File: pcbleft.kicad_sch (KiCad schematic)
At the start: 38 parts, among them SW1 GENERIC_ELECTROMECHANICAL_PUS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, SW10 GENERIC_ELECTROMECHANICAL_PUS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, SW11 GENERIC_ELECTROMECHANICAL_PUS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, SW12 GENERIC_ELECTROMECHANICAL_PUS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, SW13 GENERIC_ELECTROMECHANICAL_PUS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, SW14 GENERIC_ELECTROMECHANICAL_PUS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, SW15 GENERIC_ELECTROMECHANICAL_PUS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, SW16 GENERIC_ELECTROMECHANICAL_PUS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, SW17 GENERIC_ELECTROMECHANICAL_PUS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, SW18 GENERIC_ELECTROMECHANICAL_PUS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, SW2 GENERIC_ELECTROMECHANICAL_PUS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, SW3 GENERIC_ELECTROMECHANICAL_PUS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, SW4 GENERIC_ELECTROMECHANICAL_PUS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, SW5 GENERIC_ELECTROMECHANICAL_PUS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, SW6 GENERIC_ELECTROMECHANICAL_PUS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, SW7 GENERIC_ELECTROMECHANICAL_PUS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, SW8 GENERIC_ELECTROMECHANICAL_PUS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, SW9 GENERIC_ELECTROMECHANICAL_PUS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, U1 XIAO-RP2040-DIP

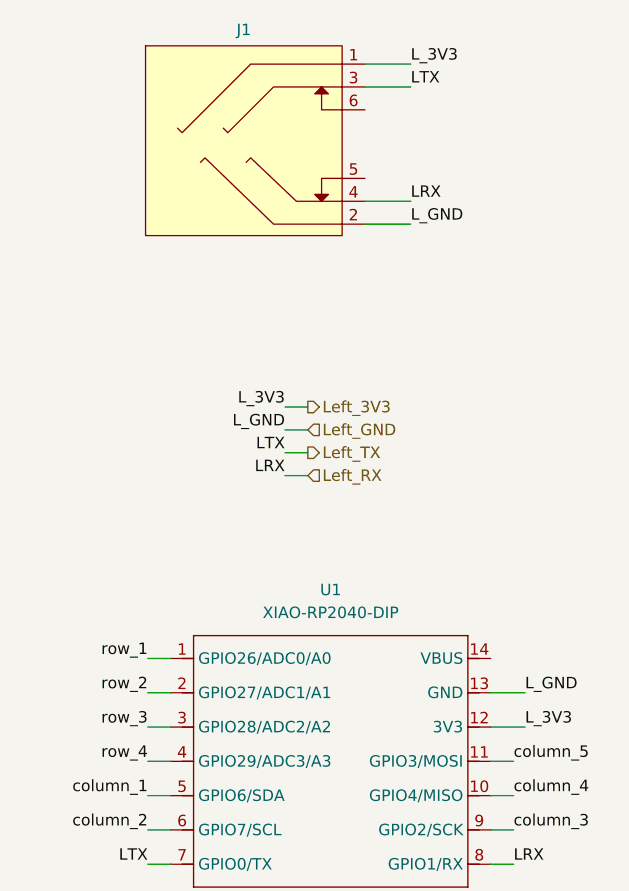
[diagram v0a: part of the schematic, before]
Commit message: Rev 1.1, fix diode footprints, add plate and base generation jobs, add mouse bites and some extra solder jumpers
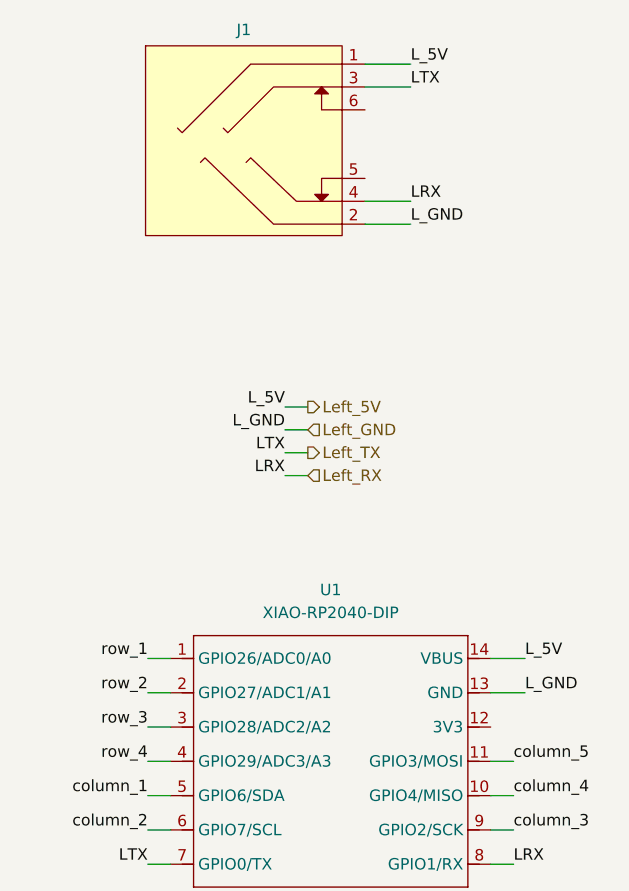
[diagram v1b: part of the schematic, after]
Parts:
- SW1, SW10, SW11, SW12, SW13, SW14, SW15, SW16, SW17, SW18, SW2, SW3, SW4, SW5, SW6, SW7, SW8, SW9: footprint benri-projects:GatereonHotswap -> benri-projects:GATEREON_KS-2P02B01-01-a_R
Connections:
- net Left_5V: now reaches U1.14 (VBUS)
- net Left_5V: now also J1.1
- net Left_3V3: no longer names the net of U1.12 (3V3)
- net Left_3V3: no longer J1.1
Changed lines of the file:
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@@
 	(wire
 		(pts
+			(xy 231.14 120.65) (xy 234.95 120.65)
+		)
+		(stroke
+			(width 0)
+			(type default)
+		)
+	)
+	(wire
+		(pts
 			(xy 135.89 71.12) (xy 135.89 73.66)
 		)
@@
 	(wire
 		(pts
-			(xy 231.14 128.27) (xy 234.95 128.27)
-		)
-		(stroke
-			(width 0)
-			(type default)
-		)
-	)
-	(wire
-		(pts
 			(xy 92.71 87.63) (xy 93.98 87.63)
 		)
@@
 		)
 	)
-	(label "L_3V3"
+	(label "L_5V"
 		(at 208.28 92.71 180)
 		(effects
@@
 		)
 	)
-	(label "L_3V3"
-		(at 234.95 128.27 0)
+	(label "L_5V"
+		(at 234.95 120.65 0)
 		(effects
 			(font
@@
 		)
 	)
-	(label "L_3V3"
+	(label "L_5V"
 		(at 222.25 54.61 0)
 		(effects
@@
 		)
 	)
-	(hierarchical_label "Left_3V3"
+	(hierarchical_label "Left_5V"
 		(shape output)
 		(at 210.82 92.71 0)
@@
 			)
 		)
-		(property "Footprint" "benri-projects:GatereonHotswap"
+		(property "Footprint" "benri-projects:GATEREON_KS-2P02B01-01-a_R"
 			(at 124.46 99.06 0)
 			(effects
@@
 			)
 		)
-		(property "Footprint" "benri-projects:GatereonHotswap"
+		(property "Footprint" "benri-projects:GATEREON_KS-2P02B01-01-a_R"
 			(at 124.46 82.55 0)
 			(effects
@@
 			)
 		)
-		(property "Footprint" "benri-projects:GatereonHotswap"
+		(property "Footprint" "benri-projects:GATEREON_KS-2P02B01-01-a_R"
 			(at 68.58 82.55 0)
 			(effects
@@
 			)
 		)
-		(property "Footprint" "benri-projects:GatereonHotswap"
+		(property "Footprint" "benri-projects:GATEREON_KS-2P02B01-01-a_R"
 			(at 87.63 82.55 0)
 			(effects
@@
 			)
 		)
-		(property "Footprint" "benri-projects:GatereonHotswap"
+		(property "Footprint" "benri-projects:GATEREON_KS-2P02B01-01-a_R"
 			(at 124.46 115.57 0)
 			(effects
@@
 			)
 		)
-		(property "Footprint" "benri-projects:GatereonHotswap"
+		(property "Footprint" "benri-projects:GATEREON_KS-2P02B01-01-a_R"
 			(at 105.41 66.04 0)
 			(effects
@@
 			)
 		)
-		(property "Footprint" "benri-projects:GatereonHotswap"
+		(property "Footprint" "benri-projects:GATEREON_KS-2P02B01-01-a_R"
 			(at 87.63 99.06 0)
 			(effects
@@
 			)
 		)
-		(property "Footprint" "benri-projects:GatereonHotswap"
+		(property "Footprint" "benri-projects:GATEREON_KS-2P02B01-01-a_R"
 			(at 105.41 99.06 0)
 			(effects
@@
 			)
 		)
-		(property "Footprint" "benri-projects:GatereonHotswap"
+		(property "Footprint" "benri-projects:GATEREON_KS-2P02B01-01-a_R"
 			(at 143.51 66.04 0)
 			(effects
@@
 			)
 		)
-		(property "Footprint" "benri-projects:GatereonHotswap"
+		(property "Footprint" "benri-projects:GATEREON_KS-2P02B01-01-a_R"
 			(at 68.58 66.04 0)
 			(effects
@@
 			)
 		)
-		(property "Footprint" "benri-projects:GatereonHotswap"
+		(property "Footprint" "benri-projects:GATEREON_KS-2P02B01-01-a_R"
 			(at 50.8 66.04 0)
 			(effects
@@
 			)
 		)
-		(property "Footprint" "benri-projects:GatereonHotswap"
+		(property "Footprint" "benri-projects:GATEREON_KS-2P02B01-01-a_R"
 			(at 124.46 66.04 0)
 			(effects
@@
 			)
 		)
-		(property "Footprint" "benri-projects:GatereonHotswap"
+		(property "Footprint" "benri-projects:GATEREON_KS-2P02B01-01-a_R"
 			(at 87.63 66.04 0)
 			(effects
@@
 			)
 		)
-		(property "Footprint" "benri-projects:GatereonHotswap"
+		(property "Footprint" "benri-projects:GATEREON_KS-2P02B01-01-a_R"
 			(at 143.51 99.06 0)
 			(effects
@@
 			)
 		)
-		(property "Footprint" "benri-projects:GatereonHotswap"
+		(property "Footprint" "benri-projects:GATEREON_KS-2P02B01-01-a_R"
 			(at 50.8 82.55 0)
 			(effects
@@
 			)
 		)
-		(property "Footprint" "benri-projects:GatereonHotswap"
+		(property "Footprint" "benri-projects:GATEREON_KS-2P02B01-01-a_R"
 			(at 105.41 82.55 0)
 			(effects
@@
 			)
 		)
-		(property "Footprint" "benri-projects:GatereonHotswap"
+		(property "Footprint" "benri-projects:GATEREON_KS-2P02B01-01-a_R"
 			(at 143.51 82.55 0)
 			(effects
@@
 			)
 		)
-		(property "Footprint" "benri-projects:GatereonHotswap"
+		(property "Footprint" "benri-projects:GATEREON_KS-2P02B01-01-a_R"
 			(at 143.51 115.57 0)
 			(effects

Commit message: Touchups and name: Logos
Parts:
- U1: footprint Seeed Studio XIAO Series Library:XIAO-RP2040-DIP -> benri-projects:SEEED_XIAO-RP2040_T-DIP
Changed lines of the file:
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@@
 			)
 		)
-		(property "Footprint" "Seeed Studio XIAO Series Library:XIAO-RP2040-DIP"
+		(property "Footprint" "benri-projects:SEEED_XIAO-RP2040_T-DIP"
 			(at 213.868 147.828 0)
 			(effects

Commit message: Latest release
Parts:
- removed J1: ~, benri-projects:TENSILITY_54-00176_R, symbol benri-projects:CONNECTOR_TENSILITY_54-00176
- added J3: (no value), symbol benri-projects:CONNECTOR_JST_SM04B-SRSS-TB
- U1: footprint benri-projects:SEEED_XIAO-RP2040_T-DIP -> Module:MOUDLE14P-XIAO-DIP-SMD
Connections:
- net Left_5V: now also J3.1
- net Left_GND: now also J3.4
- net Left_RX: now also J3.3
- net Left_TX: now also J3.2

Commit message: Through hole layout
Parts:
- removed J3: (no value), symbol benri-projects:CONNECTOR_JST_SM04B-SRSS-TB
- D1, D10, D11, D12, D13, D14, D15, D16, D17, D18, D2, D3, D4, D5, D6, D7, D8, D9: footprint benri-projects:DIODES_SOD232_R -> benri-projects:GENERIC_DO-35_A
- U1: footprint Module:MOUDLE14P-XIAO-DIP-SMD -> benri-projects:SEEED_XIAO-RP2040_T-DIP
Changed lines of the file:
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@@
 	(wire
 		(pts
-			(xy 214.63 85.09) (xy 219.71 85.09)
-		)
-		(stroke
-			(width 0)
-			(type default)
-		)
-	)
-	(wire
-		(pts
 			(xy 116.84 95.25) (xy 116.84 96.52)
 		)
@@
 	(wire
 		(pts
-			(xy 214.63 87.63) (xy 219.71 87.63)
-		)
-		(stroke
-			(width 0)
-			(type default)
-		)
-	)
-	(wire
-		(pts
 			(xy 40.64 129.54) (xy 116.84 129.54)
 		)
@@
 	(wire
 		(pts
-			(xy 214.63 82.55) (xy 219.71 82.55)
-		)
-		(stroke
-			(width 0)
-			(type default)
-		)
-	)
-	(wire
-		(pts
 			(xy 92.71 87.63) (xy 93.98 87.63)
 		)
@@
 	(wire
 		(pts
-			(xy 214.63 80.01) (xy 219.71 80.01)
-		)
-		(stroke
-			(width 0)
-			(type default)
-		)
-	)
-	(wire
-		(pts
 			(xy 74.93 64.77) (xy 74.93 71.12)
 		)
@@
 		)
 	)
-	(label "L_GND"
-		(at 219.71 87.63 0)
-		(effects
-			(font
-				(size 1.27 1.27)
-			)
-			(justify left bottom)
-		)
-	)
 	(label "row_2"
 		(at 193.04 124.46 180)
@@
 		)
 	)
-	(label "LRX"
-		(at 219.71 85.09 0)
-		(effects
-			(font
-				(size 1.27 1.27)
-			)
-			(justify left bottom)
-		)
-	)
-	(label "LTX"
-		(at 219.71 82.55 0)
-		(effects
-			(font
-				(size 1.27 1.27)
-			)
-			(justify left bottom)
-		)
-	)
 	(label "column_4"
 		(at 233.68 135.89 0)
@@
 		)
 	)
-	(label "L_5V"
-		(at 219.71 80.01 0)
-		(effects
-			(font
-				(size 1.27 1.27)
-			)
-			(justify left bottom)
-		)
-	)
 	(label "row_4"
 		(at 158.75 129.54 0)
@@
 			)
 		)
-		(property "Footprint" "Module:MOUDLE14P-XIAO-DIP-SMD"
+		(property "Footprint" "benri-projects:SEEED_XIAO-RP2040_T-DIP"
 			(at 213.868 147.828 0)
 			(hide yes)
@@
 			)
 		)
-		(property "Footprint" "benri-projects:DIODES_SOD232_R"
+		(property "Footprint" "benri-projects:GENERIC_DO-35_A"
 			(at 90.17 92.71 0)
 			(hide yes)
@@
 			)
 		)
-		(property "Footprint" "benri-projects:DIODES_SOD232_R"
+		(property "Footprint" "benri-projects:GENERIC_DO-35_A"
 			(at 127 109.22 0)
 			(hide yes)
@@
 			)
 		)
-		(property "Footprint" "benri-projects:DIODES_SOD232_R"
+		(property "Footprint" "benri-projects:GENERIC_DO-35_A"
 			(at 107.95 92.71 0)
 			(hide yes)
@@
 			)
 		)
-		(property "Footprint" "benri-projects:DIODES_SOD232_R"
+		(property "Footprint" "benri-projects:GENERIC_DO-35_A"
 			(at 127 76.2 0)
 			(hide yes)
@@
 			)
 		)
-		(property "Footprint" "benri-projects:DIODES_SOD232_R"
+		(property "Footprint" "benri-projects:GENERIC_DO-35_A"
 			(at 107.95 109.22 0)
 			(hide yes)
@@
 			)
 		)
-		(property "Footprint" "benri-projects:DIODES_SOD232_R"
+		(property "Footprint" "benri-projects:GENERIC_DO-35_A"
 			(at 146.05 125.73 0)
 			(hide yes)
@@
 			)
 		)
-		(property "Footprint" "benri-projects:DIODES_SOD232_R"
+		(property "Footprint" "benri-projects:GENERIC_DO-35_A"
 			(at 146.05 76.2 0)
 			(hide yes)
@@
 			)
 		)
-		(property "Footprint" "benri-projects:DIODES_SOD232_R"
+		(property "Footprint" "benri-projects:GENERIC_DO-35_A"
 			(at 146.05 109.22 0)
 			(hide yes)
@@
 			)
 		)
-		(property "Footprint" "benri-projects:DIODES_SOD232_R"
+		(property "Footprint" "benri-projects:GENERIC_DO-35_A"
 			(at 90.17 109.22 0)
 			(hide yes)
@@
 			)
 		)
-		(property "Footprint" "benri-projects:DIODES_SOD232_R"
+		(property "Footprint" "benri-projects:GENERIC_DO-35_A"
 			(at 53.34 76.2 0)
 			(hide yes)
@@
 			)
 		)
-		(property "Footprint" "benri-projects:DIODES_SOD232_R"
+		(property "Footprint" "benri-projects:GENERIC_DO-35_A"
 			(at 71.12 76.2 0)
 			(hide yes)
@@
 			)
 		)
-		(property "Footprint" "benri-projects:DIODES_SOD232_R"
+		(property "Footprint" "benri-projects:GENERIC_DO-35_A"
 			(at 127 125.73 0)
 			(hide yes)
@@
 			)
 		)
-		(property "Footprint" "benri-projects:DIODES_SOD232_R"
+		(property "Footprint" "benri-projects:GENERIC_DO-35_A"
 			(at 53.34 92.71 0)
 			(hide yes)
@@
 	)
 	(symbol
-		(lib_id "benri-projects:CONNECTOR_JST_SM04B-SRSS-TB")
-		(at 209.55 83.82 0)
-		(mirror y)
-		(unit 1)
-		(body_style 1)
-		(exclude_from_sim no)
-		(in_bom yes)
-		(on_board yes)
-		(in_pos_files yes)
-		(dnp no)
-		(fields_autoplaced yes)
-		(property "Reference" "J3"
-			(at 209.55 76.2 0)
-			(show_name no)
-			(do_not_autoplace no)
-			(effects
-				(font
-					(size 1.27 1.27)
-				)
-			)
-		)
-		(property "Value" ""
-			(at 209.55 83.82 0)
-			(show_name no)
-			(do_not_autoplace no)
-			(effects
-				(font
-					(size 1.27 1.27)
-				)
-			)
-		)
-		(property "Footprint" ""
-			(at 209.55 83.82 0)
-			(hide yes)
-			(show_name no)
-			(do_not_autoplace no)
-			(effects
-				(font
-					(size 1.27 1.27)
-				)
-			)
-		)
-		(property "Datasheet" ""
-			(at 209.55 83.82 0)
-			(hide yes)
-			(show_name no)
-			(do_not_autoplace no)
-			(effects
-				(font
-					(size 1.27 1.27)
-				)
-			)
-		)
-		(property "Description" ""
-			(at 209.55 83.82 0)
-			(hide yes)
-			(show_name no)
-			(do_not_autoplace no)
-			(effects
-				(font
-					(size 1.27 1.27)
-				)
-			)
-		)
-		(pin "1"
-		)
-		(pin "2"
-		)
-		(pin "3"
-		)
-		(pin "4"
-		)
-		(instances
-			(project "keyboard-split-splay-5x3+2-pinky-cluster"
-				(path "/81ff113e-ae40-4f69-bd5b-ccd6a1ee23eb/db6b093a-3758-4fce-8b5b-f9958eb097a6"
-					(reference "J3")
-					(unit 1)
-				)
-			)
-		)
-	)
-	(symbol
 		(lib_id "benri-projects:GENERIC_DIODE")
 		(at 80.01 76.2 90)
@@
 			)
 		)
-		(property "Footprint" "benri-projects:DIODES_SOD232_R"
+		(property "Footprint" "benri-projects:GENERIC_DO-35_A"
 			(at 90.17 76.2 0)
 			(hide yes)
@@
 			)
 		)
-		(property "Footprint" "benri-projects:DIODES_SOD232_R"
+		(property "Footprint" "benri-projects:GENERIC_DO-35_A"
 			(at 127 92.71 0)
 			(hide yes)
@@
 			)
 		)
-		(property "Footprint" "benri-projects:DIODES_SOD232_R"
+		(property "Footprint" "benri-projects:GENERIC_DO-35_A"
 			(at 107.95 76.2 0)
 			(hide yes)
@@
 			)
 		)
-		(property "Footprint" "benri-projects:DIODES_SOD232_R"
+		(property "Footprint" "benri-projects:GENERIC_DO-35_A"
 			(at 71.12 92.71 0)
 			(hide yes)
@@
 			)
 		)
-		(property "Footprint" "benri-projects:DIODES_SOD232_R"
+		(property "Footprint" "benri-projects:GENERIC_DO-35_A"
 			(at 146.05 92.71 0)
 			(hide yes)
